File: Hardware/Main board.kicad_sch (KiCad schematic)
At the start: 36 parts, among them U1 ESP32-S3, Y1 R940000171

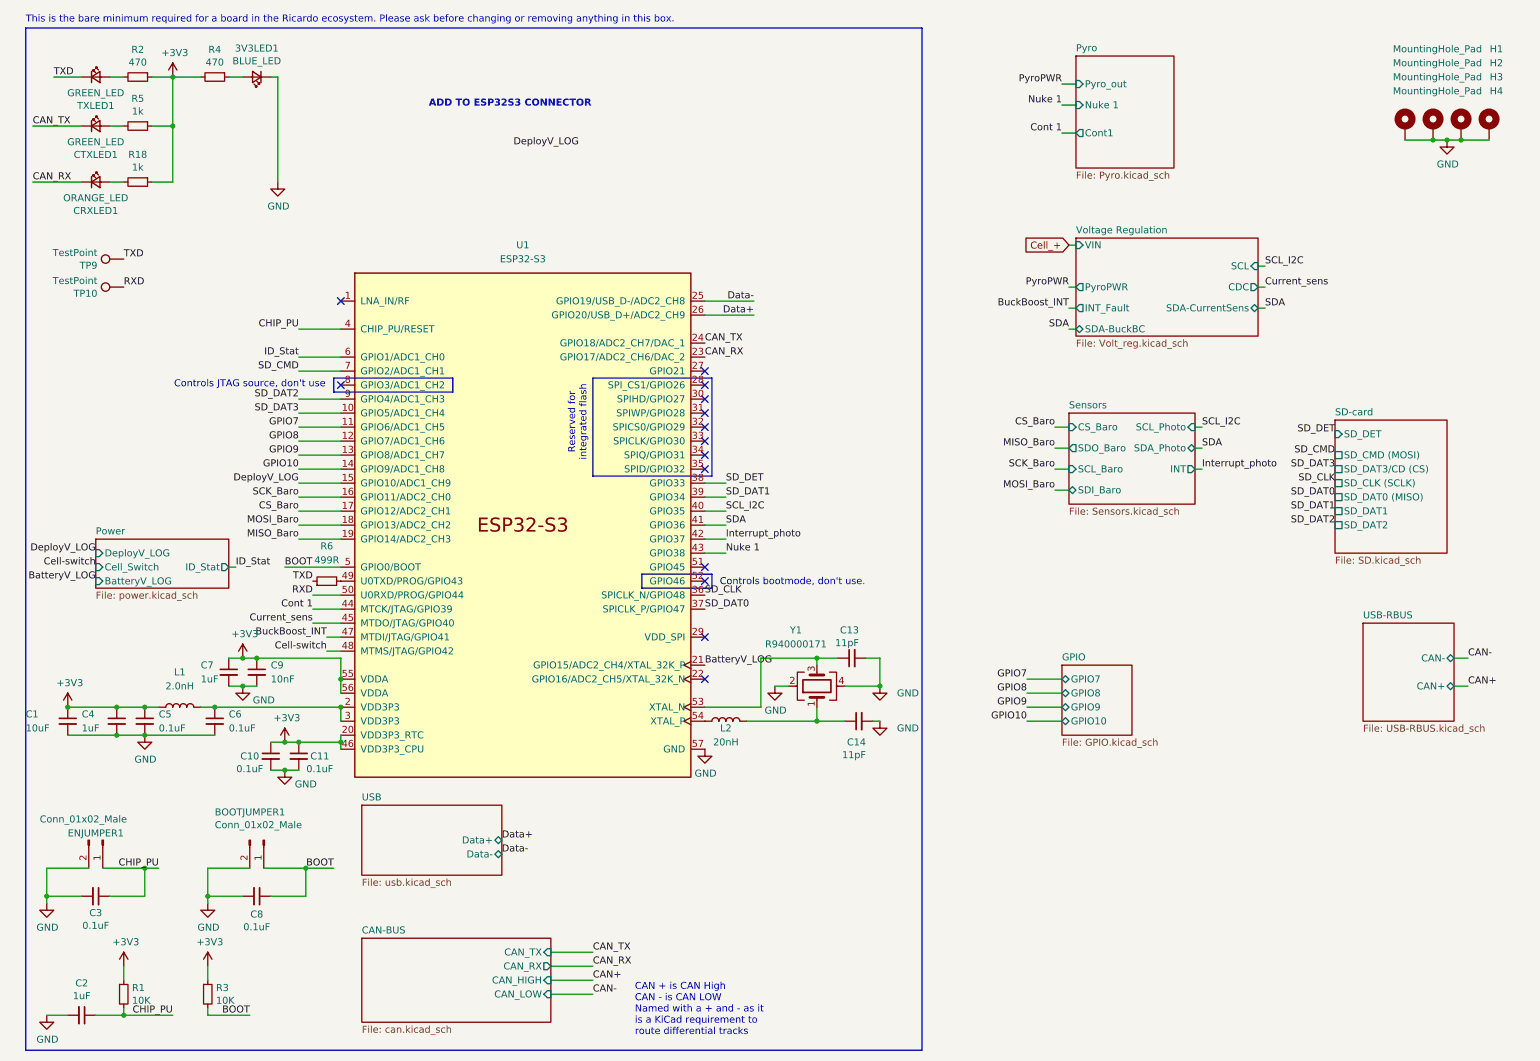
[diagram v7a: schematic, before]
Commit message: V2 hardware changes
- Removed current sensor IC
- Removed photo sensor IC
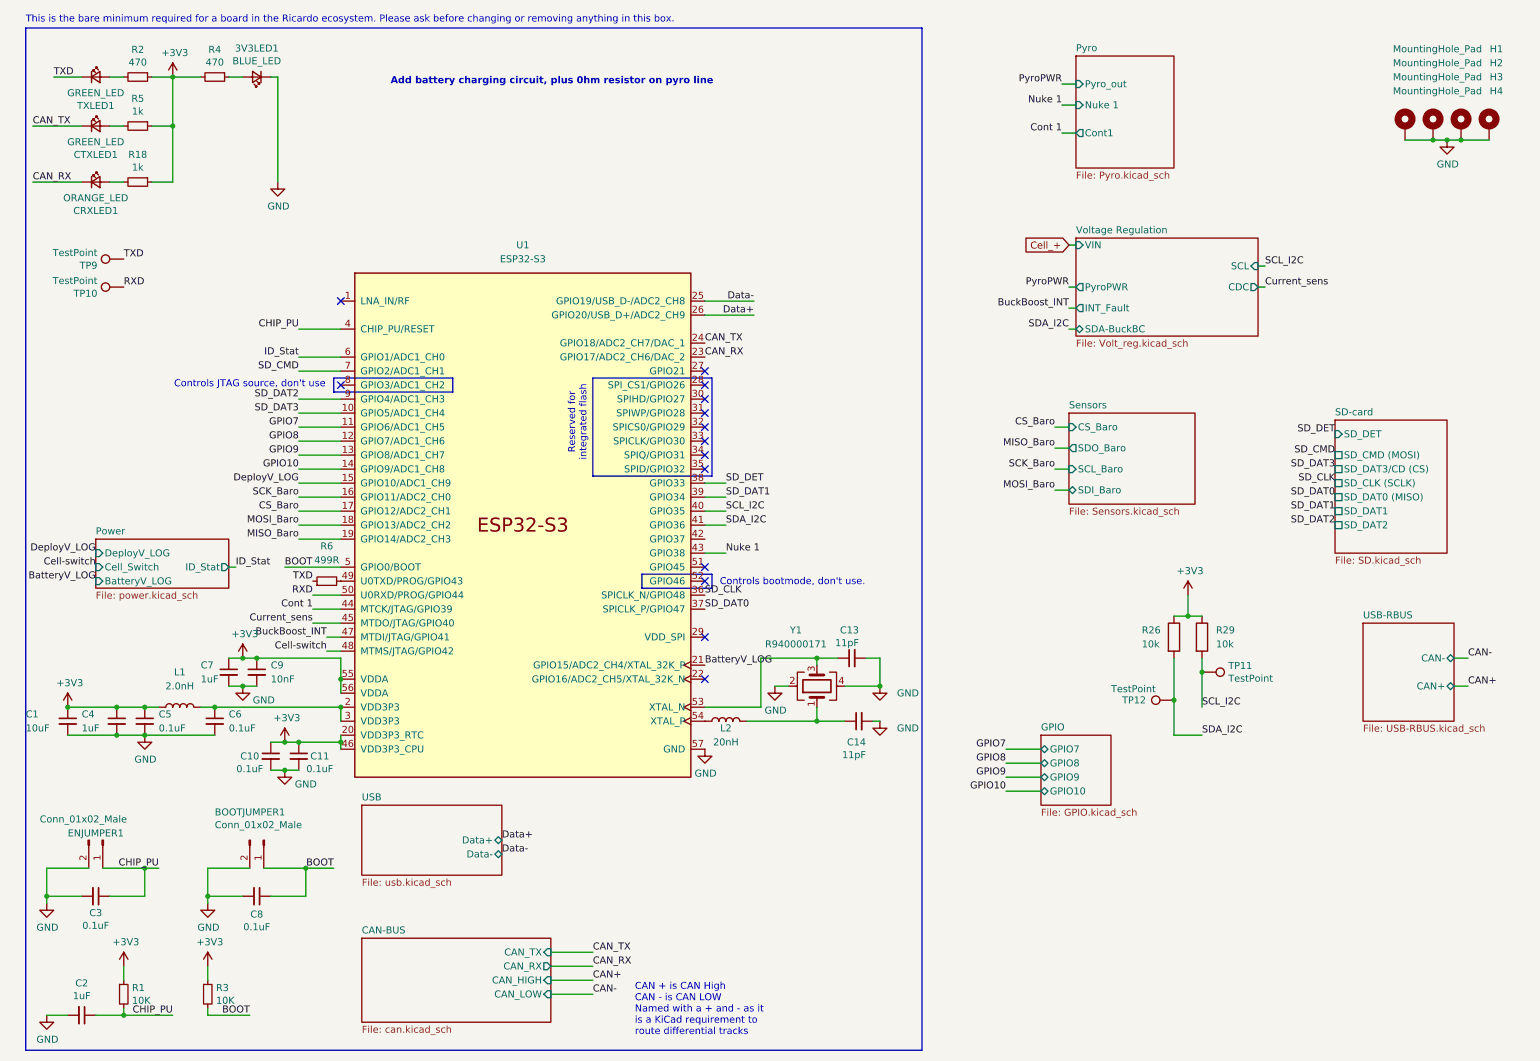
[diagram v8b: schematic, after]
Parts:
- added R26, R29: 10k, Resistor_SMD:R_0402_1005Metric, symbol Device:R
- added TP11, TP12: TestPoint, TestPoint:TestPoint_Pad_D1.0mm, symbol Connector:TestPoint
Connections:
- net +3V3: now also R26.1, R29.1
- net SCL_I2C: now also R29.2, TP11.1
- net Interrupt_photo: no longer names the net of U1.42 (GPIO37)
- net SDA renamed SDA_I2C
- net SDA_I2C: now also R26.2, TP12.1
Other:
- sheet Sensors ports: added none; removed INT, SCL_Photo, SDA_Photo
- sheet Voltage Regulation ports: added none; removed SDA-CurrentSens
- note added: "Add battery charging circuit, plus 0hm resistor on pyro line"
- note removed: "ADD TO ESP32S3 CONNECTOR"
